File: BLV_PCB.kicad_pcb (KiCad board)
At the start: 4 copper layers, 90 x 90 mm, 103 parts, among them J1 JST-PH, J12 PinHeader_01x03_Pin, J2 JST-PH, J3 JST-PH, J31 PinHeader_01x02_Pin, J4 PinHeader_01x03_Pin, J5 PinHeader_01x03_Pin, J6 PinHeader_01x03_Pin, J61 USB_C_USB2.0_16P, J62 Micro_SD_Card, J8 USB_C_USB2.0_16P, Q1 Si2301CDS, Q2 Si2301CDS, SW11 KMR2, SW12 KMR2, SW61 KMR2, U11 W25Q128JVS, U12 RP2350_60QFN, U3 TPS63001DRCR, U4 BH-18650-A6AJ012, U51 E32-400M30S, U61 NEO-M9N, Y11 ABM8_262_T3

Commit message: Add 10k pull-ups to SDcard
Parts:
- removed R1, R2: 10k, Resistor_SMD:R_0402_1005Metric
- added J7: Conn_02x03_Odd_Even, Connector_PinHeader_2.54mm:PinHeader_2x03_P2.54mm_Vertical, F.Cu at (160.5, 101.4)
- added R64: 10k, Resistor_SMD:R_0402_1005Metric, F.Cu at (153.9, 97.6)
- added RN61: 10k, Resistor_SMD:R_Array_Concave_4x0603, F.Cu at (139.2, 113.2)
- TP61: renamed from TP65; value TestPoint -> TP_DAT1
- TP62: renamed from TP66; value TestPoint -> TP_DAT2
- moved TP62 2.00 mm to (135.0, 113.0)
- renumbered C66 to C61, C61 to C62, C65 to C63, C62 to C64, C63 to C65, C64 to C66, R66 to R61, R61 to R62, R62 to R63, R64 to R65, R65 to R66, R63 to R67, TP61 to TP63, TP62 to TP64, TP63 to TP65, TP64 to TP66
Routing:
- net /GNSS & MicroSD/SPI_MOSI: track 68.1 -> 81.6 mm, vias 2 -> 4
- net /GNSS & MicroSD/SPI_MISO: track 63.3 -> 75.8 mm, vias 2 -> 4
- net /GNSS & MicroSD/SPI_CS0: track 42.9 -> 49.7 mm
- net /GNSS & MicroSD/DAT2: track 6.50 -> 7.45 mm
- net GND: vias 333 -> 329

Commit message: rough power layout
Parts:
- added Q3: CSD25402Q3A, Package_SON:VSON-8_3.3x3.3mm_P0.65mm_NexFET, F.Cu at (164.9, 45.4)
- added Q4: CSD25402Q3A, Package_SON:VSON-8_3.3x3.3mm_P0.65mm_NexFET, F.Cu at (190.2, 45.5)
- added U1: BQ29707, Package_SON:WSON-6_1.5x1.5mm_P0.5mm, F.Cu at (191.5, 112.5)
- added U2: MCP73833-xxx-MF, Package_DFN_QFN:DFN-10-1EP_3x3mm_P0.5mm_EP1.58x2.35mm, F.Cu at (183.9, 42.5)
- added U6: INA260, Package_SO:TSSOP-16_4.4x5mm_P0.65mm, F.Cu at (178.0, 50.5)
- L2: value 2u2 -> VLS4012ET-2R2M
- Q1, Q2: value Si2301CDS -> CSD16406Q3; footprint Package_TO_SOT_SMD:SOT-23 -> Package_TO_SOT_SMD:TDSON-8-1
- R26, R27, R28: value 1k -> 1.5k
- moved Q2 74.6 mm to (189.2, 122.6), turned to 180 degrees
- moved Q1 68.7 mm to (189.2, 116.7), turned to 180 degrees
- moved D4 19.3 mm to (169.0, 67.4), turned to 90 degrees
- moved R35 16.1 mm to (169.0, 63.9), turned to -90 degrees
- moved R32 10.5 mm to (167.5, 48.5), turned to -90 degrees
- moved C30 10.1 mm to (166.0, 48.0)
- moved C34 10.0 mm to (166.0, 59.0)
- moved C35 10.0 mm to (166.0, 60.5)
- moved C33 9.96 mm to (162.2, 56.3)
- moved C32 9.96 mm to (166.0, 52.0)
- moved L2 9.96 mm to (170.0, 56.0)
- moved R34 9.96 mm to (162.2, 54.2)
- moved U3 9.96 mm to (165.1, 56.0)
- moved R61 3.50 mm to (182.5, 112.5)
- moved SW61 3.50 mm to (179.0, 112.5)
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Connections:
- C30 pad 2: /Power/Vin -> /Power/V_SWITCH
- C31 pad 1: +BATT -> CELL+
- C31 pad 2: /Power/Vin -> /Power/V_SWITCH
- C32 pad 1: /Power/Vin -> /Power/Monitor_out
- Q1 pad 1: /Power/Vin -> CELL-
- Q1 pad 2: VBUS -> CELL-
- Q1 pad 3: /Power/Vin -> CELL-
- Q2 pad 1: /Power/Vin -> GND
- Q2 pad 2: +BATT -> GND
- Q2 pad 3: /Power/Vin -> GND
- R32 pad 1: /Power/Vin -> /Power/V_SWITCH
- R33 pad 1: /Power/Vin -> /Power/V_SWITCH
- R34 pad 1: /Power/Vin -> /Power/Monitor_out
- U12 pad 42: unconnected-(U12-GPIO28_ADC2-Pad42) -> /MCU/I2C0_SDA
- U12 pad 43: unconnected-(U12-GPIO29_ADC3-Pad43) -> /MCU/I2C0_SCL
- U3 pad 5: /Power/Vin -> /Power/Monitor_out
- U4 pad 1: GND -> CELL-
- U4 pad 2: +BATT -> CELL+
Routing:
- net VBUS: track 0.00 -> 20.3 mm
- net /Power/Monitor_out: track 0.00 -> 6.45 mm, vias 0 -> 2
- net /Power/Vin: track 6.45 -> 0.00 mm, vias 2 -> 0
- net /MCU/RF_IRQ: track 7.76 -> 14.1 mm
- net CELL+: track 0.00 -> 4.62 mm, vias 0 -> 16
- net /GNSS & MicroSD/GNSS_RST: track 22.1 -> 18.6 mm
- net GND: track 17.3 -> 20.3 mm, vias 329 -> 304
- net /MCU/RF_SPI_MISO: track 11.7 -> 14.3 mm
- net /MCU/RF_SPI_CS: track 18.1 -> 20.6 mm
- net /MCU/RF_SPI_MOSI: track 13.5 -> 15.9 mm
- net /MCU/RF_SPI_SCK: track 15.6 -> 17.5 mm
- net /MCU/RF_RST: track 9.90 -> 11.6 mm
- net /GNSS & MicroSD/VDD_USB: track 30.7 -> 29.2 mm
- net /GNSS & MicroSD/USB2_D+: track 21.3 -> 19.8 mm
- net /GNSS & MicroSD/USB2_D-: track 20.5 -> 19.0 mm
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- added copper zone on B.Cu, net CELL+
- added copper zone on F.Cu, net CELL+
- removed copper zone on B.Cu, net +BATT
- removed copper zone on F.Cu, net +BATT
- removed copper zone on F.Cu, net /Power/Vin

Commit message: 050326 layouts
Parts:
- added C31: 0.1u, Capacitor_SMD:C_0402_1005Metric, F.Cu at (113.9, 70.6)
- added C32: 1u, Capacitor_SMD:C_0603_1608Metric, F.Cu at (107.5, 70.8)
- added C33: 1u, Capacitor_SMD:C_0603_1608Metric, F.Cu at (107.5, 73.3)
- added C36: 10u, Capacitor_SMD:C_0603_1608Metric, F.Cu at (107.5, 75.8)
- added C38: 1u, Capacitor_SMD:C_0402_1005Metric, F.Cu at (113.9, 72.5)
- added C40: 10p, Capacitor_SMD:C_0402_1005Metric, F.Cu at (113.9, 74.5)
- added C41: 22u, Capacitor_SMD:C_0805_2012Metric, F.Cu at (101.0, 77.1)
- added C43: 22u, Capacitor_SMD:C_0805_2012Metric, F.Cu at (101.0, 80.2)
- added C45: 22u, Capacitor_SMD:C_0805_2012Metric, F.Cu at (101.0, 83.2)
- added C51: 10u, Capacitor_SMD:C_0603_1608Metric, F.Cu at (119.3, 58.7)
- added C52: 10u, Capacitor_SMD:C_0603_1608Metric, F.Cu at (119.3, 61.2)
- added D31: LED, LED_SMD:LED_0805_2012Metric, F.Cu at (107.8, 58.9)
- added D32: LED, LED_SMD:LED_0805_2012Metric, F.Cu at (107.8, 62.0)
- added D33: LED, LED_SMD:LED_0805_2012Metric, F.Cu at (107.8, 65.0)
- added D34: KT-0805G, LED_SMD:LED_0805_2012Metric, F.Cu at (107.8, 68.1)
- added L31: XAL7030-102ME, Inductor_SMD:L_Coilcraft_XAL7030-102, F.Cu at (185.4, 63.6)
- added R1: 10k, Resistor_SMD:R_0402_1005Metric, F.Cu at (118.8, 65.4)
- added R2: 10k, Resistor_SMD:R_0402_1005Metric, F.Cu at (118.8, 67.4)
- added R31: 330, Resistor_SMD:R_0603_1608Metric, F.Cu at (107.5, 78.4)
- added R34: 2.2k, Resistor_SMD:R_0402_1005Metric, F.Cu at (111.0, 70.6)
- added R35: 2k, Resistor_SMD:R_0402_1005Metric, F.Cu at (111.0, 72.6)
- added R36: 2k, Resistor_SMD:R_0402_1005Metric, F.Cu at (111.0, 74.5)
- added R37: 2k, Resistor_SMD:R_0402_1005Metric, F.Cu at (111.0, 76.5)
- added R38: 2k, Resistor_SMD:R_0402_1005Metric, F.Cu at (111.0, 78.5)
- added R39: 10k, Resistor_SMD:R_0402_1005Metric, F.Cu at (111.0, 80.5)
- added R43: 1M, Resistor_SMD:R_0402_1005Metric, F.Cu at (111.0, 82.5)
- added R44: 330k, Resistor_SMD:R_0402_1005Metric, F.Cu at (111.0, 84.5)
- added R45: 2k, Resistor_SMD:R_0603_1608Metric, F.Cu at (107.5, 80.9)
- added SW31: K3-1391B-51, Slide_Switch:SW-TH_K3-1391B-51, F.Cu at (178.0, 46.7)
- added U35: TPS61236PRWLR, TPS61236:VQFN-9_L2.5-W2.5-P0.50-TL, F.Cu at (185.0, 57.7)
- U33: renamed from U2; value MCP73833-xxx-MF -> MCP73833-FCI-MF
- moved U33 40.3 mm to (147.5, 25.3)
- moved U34 9.55 mm to (177.0, 60.0)
- renumbered C30 to C34, C31 to C35, C32 to C37, C33 to C39, C34 to C42, C35 to C44, D4 to D35, J8 to J31, J31 to J32, L2 to L32, Q1 to Q31, Q2 to Q32, Q3 to Q33, Q4 to Q34, R30 to R32, R31 to R33, R32 to R40, R33 to R41, R34 to R42, R35 to R46, U4 to U31, U1 to U32, U6 to U34, U3 to U36
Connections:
- U51 pad 10: +3V3 -> +5V
- U51 pad 9: +3V3 -> +5V
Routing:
- net VBUS: track 20.3 -> 0.00 mm
- net CELL+: track 4.62 -> 0.00 mm
- net GND: vias 304 -> 303

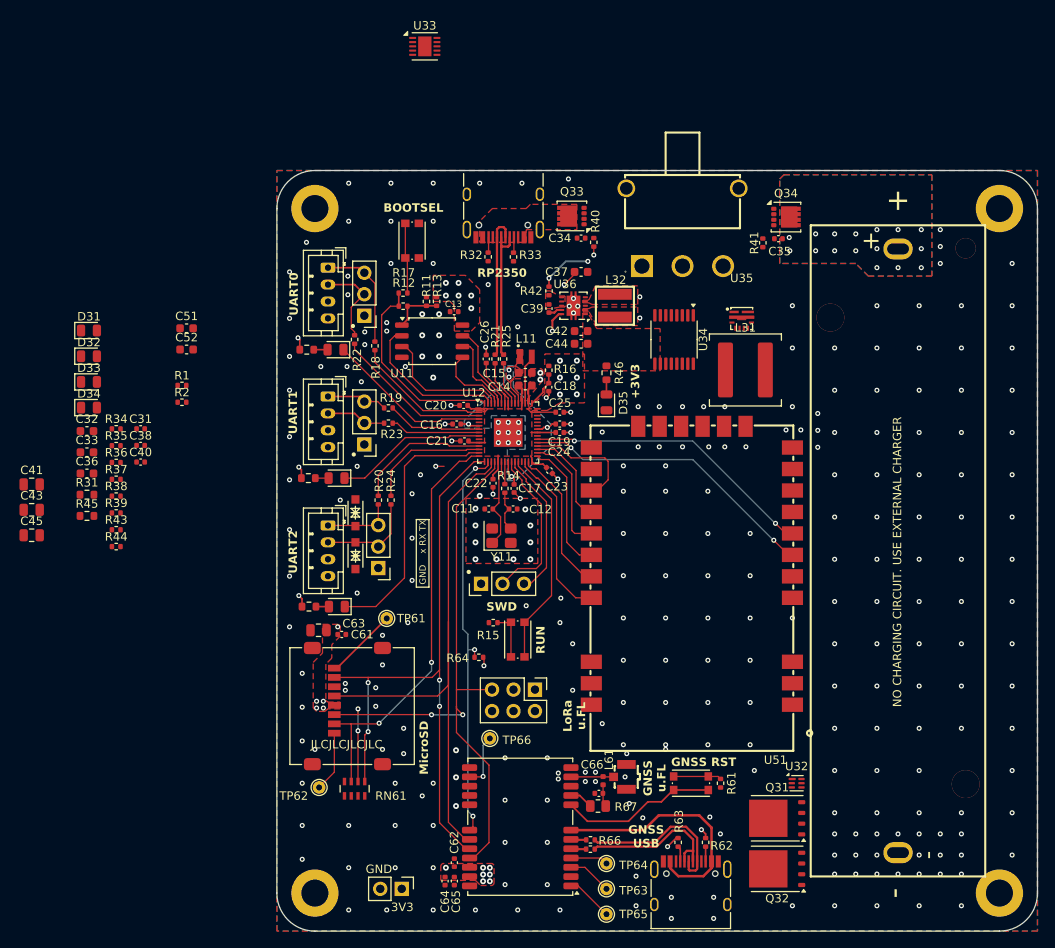
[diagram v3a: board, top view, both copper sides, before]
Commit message: Finish preliminary power layout
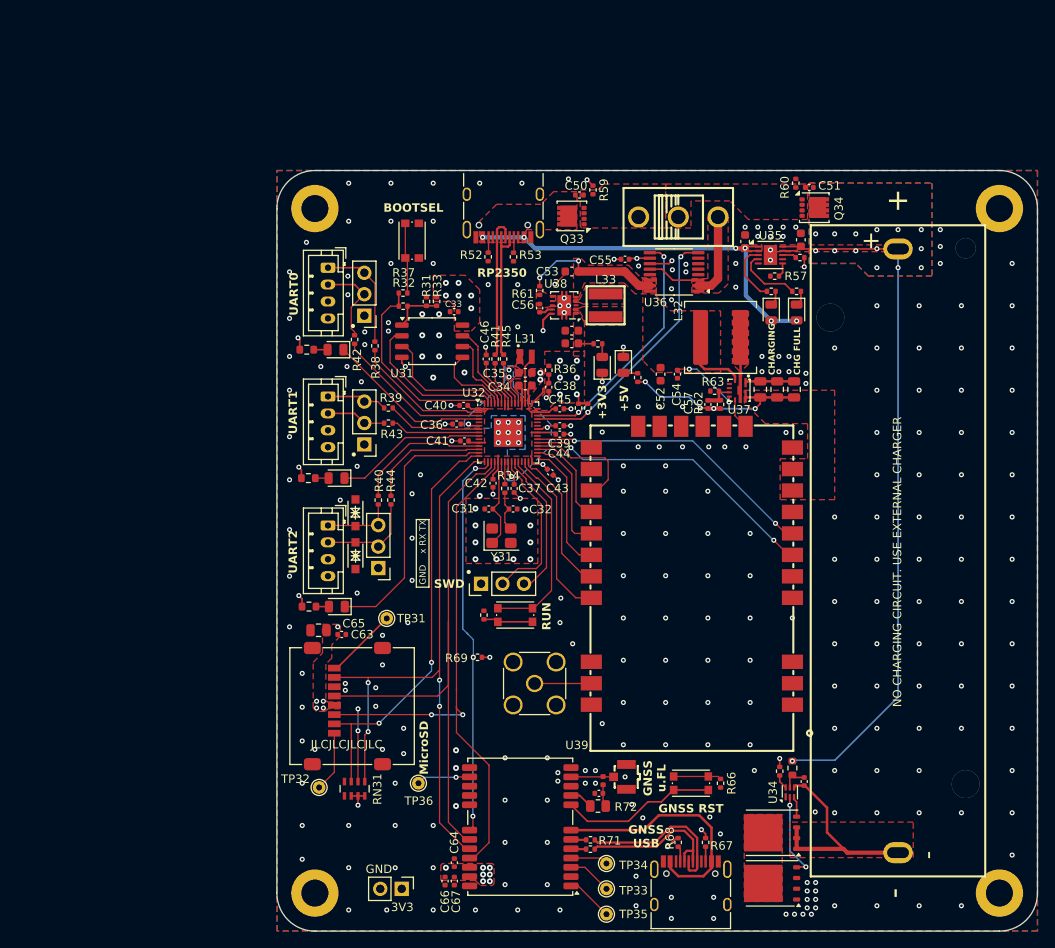
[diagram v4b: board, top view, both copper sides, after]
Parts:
- removed the C51 at (119.3, 58.7)
- removed the C52 at (119.3, 61.2)
- removed the D33 at (107.8, 65.0)
- removed J7: Conn_02x03_Odd_Even, Connector_PinHeader_2.54mm:PinHeader_2x03_P2.54mm_Vertical
- removed the R37 at (111.0, 76.5)
- removed the SW31 at (178.0, 46.7)
- added C55: 100n, Capacitor_SMD:C_0402_1005Metric, F.Cu at (171.2, 50.5)
- added J40: Conn_Coaxial, Connector_Coaxial:SMA_Amphenol_132134_Vertical, F.Cu at (160.5, 100.7)
- added SW33: SS-12D10L9, Slide_Switch:SW-TH_SS-12D10L9, F.Cu at (177.5, 45.5)
- D36: renamed from D31; value LED -> KT-0805Y
- D37: renamed from D32; value LED -> KT-0805G
- R55: renamed from R35; value 2k -> 2.2k
- R56: renamed from R36; value 2k -> 2.2k
- R64: renamed from R45; value 2k -> 2.2k; footprint Resistor_SMD:R_0603_1608Metric -> Resistor_SMD:R_0402_1005Metric
- R65: renamed from R46; footprint Resistor_SMD:R_0603_1608Metric -> Resistor_SMD:R_0402_1005Metric
- moved C62 91.8 mm to (191.2, 65.9), turned to 90 degrees
- moved R51 89.5 mm to (191.0, 110.7), turned to -90 degrees
- moved C60 89.4 mm to (189.2, 65.9), turned to 90 degrees
- moved C47 88.9 mm to (192.4, 112.3), turned to -90 degrees
- moved R54 88.3 mm to (189.5, 111.1), turned to 90 degrees
- moved C49 88.1 mm to (192.0, 48.2), turned to 90 degrees
- moved C58 86.9 mm to (187.2, 65.9), turned to 90 degrees
- moved R58 86.4 mm to (191.9, 50.3)
- moved D37 83.9 mm to (191.5, 56.8), turned to -90 degrees
- moved R56 83.0 mm to (191.5, 54.3), turned to 180 degrees
- moved R57 82.1 mm to (188.9, 52.5), turned to 180 degrees
- moved C48 81.0 mm to (185.4, 48.4), turned to 90 degrees
- moved D36 80.8 mm to (188.5, 56.8), turned to -90 degrees
- moved R55 79.6 mm to (188.5, 54.3), turned to 180 degrees
- moved R63 73.2 mm to (181.8, 66.1), turned to 180 degrees
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- renumbered C11 to C31, C12 to C32, C13 to C33, C14 to C34, C15 to C35, C16 to C36, C17 to C37, C18 to C38, C19 to C39, C20 to C40, C21 to C41, C22 to C42, C23 to C43, C24 to C44, C25 to C45, C26 to C46, C31 to C47, C32 to C48, C33 to C49, C34 to C50, C35 to C51, C36 to C52, C37 to C53, C38 to C54, C39 to C56, C40 to C57, C41 to C58, C42 to C59, C43 to C60, C44 to C61, C45 to C62, C61 to C63, C62 to C64, C63 to C65, C64 to C66, C65 to C67, C66 to C68, D1 to D31, D2 to D32, D11 to D33, D12 to D34, D13 to D35, D34 to D38, D35 to D39, H1 to H31, H2 to H32, H3 to H33, H4 to H34, J1 to J31, J2 to J32, J3 to J33, J6 to J34, J4 to J35, J5 to J36, J12 to J37, J31 to J38, J32 to J39, J61 to J41, J62 to J42, JP61 to JP31, L11 to L31, L31 to L32, L32 to L33, L61 to L34, R11 to R31, R12 to R32, R13 to R33, R14 to R34, R15 to R35, R16 to R36, R17 to R37, R18 to R38, R19 to R39, R20 to R40, R21 to R41, R22 to R42, R23 to R43, R24 to R44, R25 to R45, R1 to R46, R2 to R47, R26 to R48, R27 to R49, R28 to R50, R31 to R51, R32 to R52, R33 to R53, R34 to R54, R38 to R57, R39 to R58, R40 to R59, R41 to R60, R42 to R61, R43 to R62, R44 to R63, R61 to R66, R62 to R67, R63 to R68, R64 to R69, R65 to R70, R66 to R71, R67 to R72, RN61 to RN31, SW11 to SW31, SW12 to SW32, SW61 to SW34, TP61 to TP31, TP62 to TP32, TP63 to TP33, TP64 to TP34, TP65 to TP35, TP66 to TP36, U11 to U31, U12 to U32, U31 to U33, U32 to U34, U33 to U35, U34 to U36, U35 to U37, U36 to U38, U51 to U39, U61 to U40, Y11 to Y31
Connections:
- net /Power/FB renamed /Power/5V_FB
- net /Power/Monitor_in renamed /Power/IN+
- net /Power/Monitor_out renamed /Power/IN-
- net /Power/SW renamed /Power/5V_SW
- U35 pad 7: /Power/~{PG} -> unconnected-(U35-~{PG}-Pad7)
- U36 pad 8: /Power/I2C0_SDA -> /MCU/I2C0_SDA
- U36 pad 9: /Power/I2C0_SCL -> /MCU/I2C0_SCL
- U39 pad 27: unconnected-(U51-ANT-Pad27) -> /RF/LoRa_ANT
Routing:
- net CELL+: track 0.00 -> 85.0 mm, vias 16 -> 15
- net VBUS: track 0.00 -> 48.6 mm, vias 0 -> 6
- net /MCU/I2C0_SDA: track 0.00 -> 31.5 mm, vias 0 -> 2
- net /MCU/I2C0_SCL: track 0.00 -> 29.5 mm, vias 0 -> 2
- net /Power/IN-: track 6.45 -> 33.8 mm, vias 2 -> 4
- net CELL-: track 0.00 -> 26.1 mm
- net +5V: track 0.00 -> 23.5 mm, vias 0 -> 4
- net GND: track 20.3 -> 38.8 mm, vias 303 -> 309
- net /Power/IN+: track 0.00 -> 16.2 mm
- net /Power/Cout: track 0.00 -> 10.3 mm, vias 0 -> 2
- net +3V3: track 36.3 -> 45.0 mm, vias 30 -> 32
- net /Power/STAT2: track 0.00 -> 7.86 mm
- net /Power/STAT1: track 0.00 -> 7.07 mm
- net /RF/LoRa_ANT: track 0.00 -> 6.72 mm
- net /Power/5V_SW: track 0.00 -> 6.26 mm
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- added copper zone on F.Cu, net +5V
- added copper zone on F.Cu, net /Power/5V_SW
- added copper zone on F.Cu, net /Power/IN+
- added copper zone on F.Cu, net /Power/IN-
- added copper zone on F.Cu, net /Power/V_SWITCH
- added copper zone on F.Cu, net CELL-
- added copper zone on F.Cu, net Net-(Q31-D)
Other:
- board text added: "+5V"
- board text added: "CHARGING"
- board text added: "CHG FULL"
- board text removed: "LoRa u.FL"

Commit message: v2 layouts done
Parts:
- added C71: 100n, Capacitor_SMD:C_0402_1005Metric, F.Cu at (144.3, 126.6)
- added U71: MCP9808_DFN, Package_DFN_QFN:DFN-8-1EP_3x2mm_P0.5mm_EP1.7x1.4mm, F.Cu at (141.7, 127.0)
- C47: value 0.1u -> 100n
- Q31, Q32: footprint Package_TO_SOT_SMD:TDSON-8-1 -> Package_SON:VSON-8_3.3x3.3mm_P0.65mm_NexFET
- R63: footprint Resistor_SMD:R_0402_1005Metric -> Resistor_SMD:R_0603_1608Metric
- moved J39 8.38 mm to (147.3, 117.0)
- moved SW31 2.03 mm to (145.7, 50.3), turned to 0 degrees
- moved Q31 1.73 mm to (189.9, 119.5)
- moved Q32 1.62 mm to (189.9, 123.4)
- moved R63 0.54 mm to (181.3, 65.9)
- moved R37 0.40 mm to (144.9, 54.9)
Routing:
- net /MCU/I2C0_SCL: track 29.5 -> 103.8 mm, vias 2 -> 3
- net /MCU/I2C0_SDA: track 31.5 -> 103.8 mm, vias 2 -> 3
- net GND: track 38.8 -> 48.0 mm, vias 309 -> 302
- net +3V3: track 45.0 -> 48.4 mm, vias 32 -> 33
- net /Power/Dout: track 2.43 -> 4.56 mm
- net CELL-: track 26.1 -> 25.1 mm
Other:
- board text added: "BLV Data, Telemetry, and LoRaLink PCB. Designed by Tri Do"
- board text added: "TEMP"
- board text removed: "BLV Data, Telemetry, and LoRaLink Board by Tri Do"

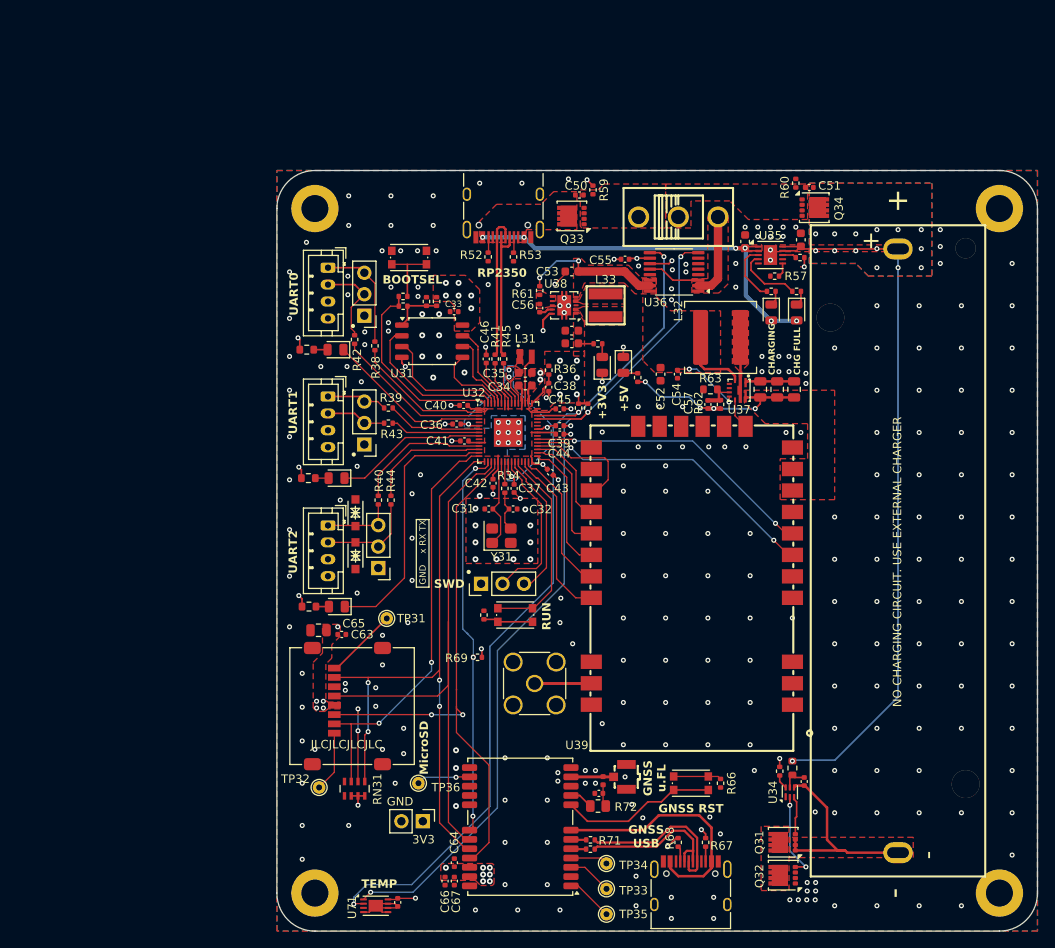
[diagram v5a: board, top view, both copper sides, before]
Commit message: Final production changes
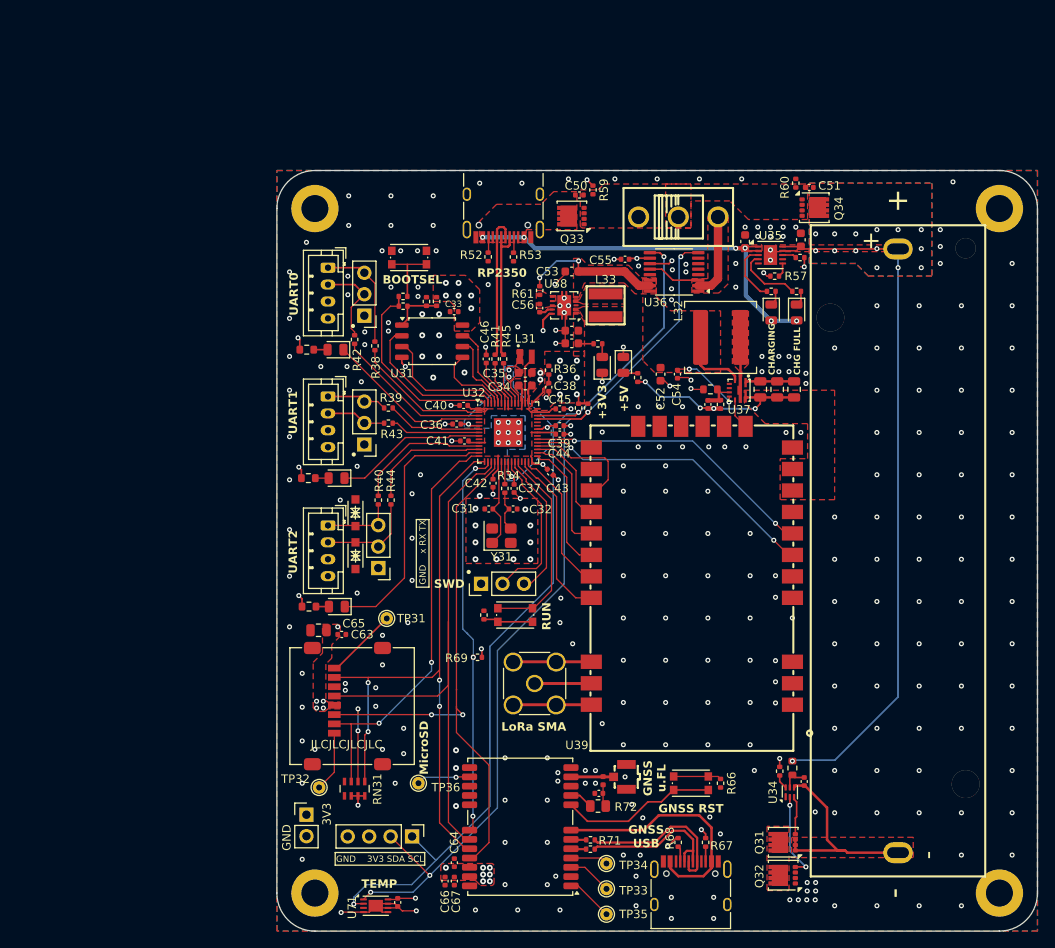
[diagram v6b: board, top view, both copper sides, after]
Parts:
- added J71: Conn_01x04_Pin, Connector_PinHeader_2.54mm:PinHeader_1x04_P2.54mm_Vertical, F.Cu at (146.0, 118.8)
- C68: value 100n X7R -> 100n
- moved J39 13.8 mm to (133.5, 116.2), turned to 0 degrees
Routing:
- net GND: track 48.0 -> 84.0 mm, vias 302 -> 322
- net /MCU/I2C0_SDA: track 103.8 -> 110.4 mm, vias 3 -> 4
- net /MCU/I2C0_SCL: track 103.8 -> 107.8 mm
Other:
- board text added: "GND 3V3 SDA SCL"
- board text added: "LoRa SMA"
- board text removed: "NO CHARGING CIRCUIT. USE EXTERNAL CHARGER"
